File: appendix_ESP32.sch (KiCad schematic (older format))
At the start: 0 parts

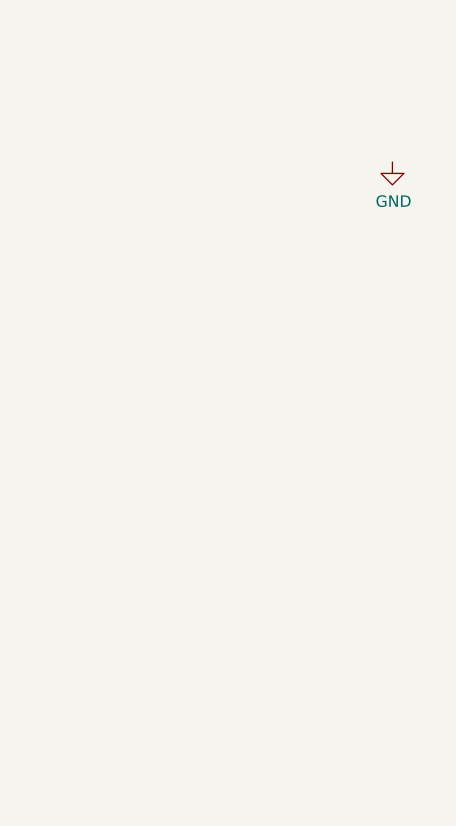
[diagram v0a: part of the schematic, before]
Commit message: added FTDI chip
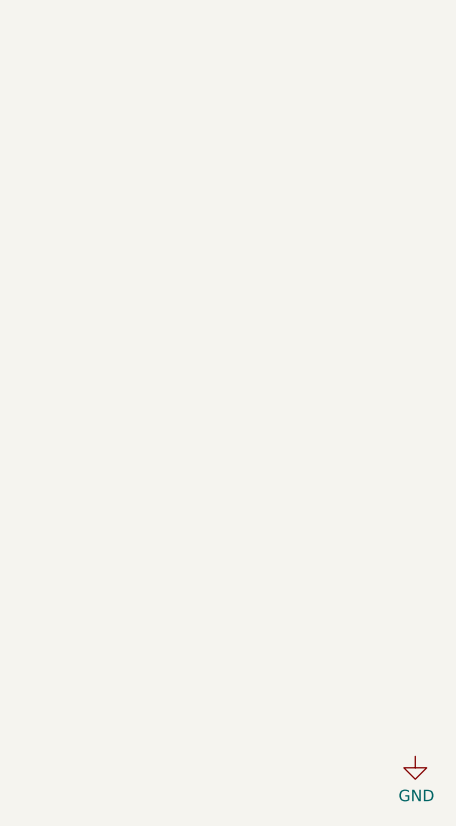
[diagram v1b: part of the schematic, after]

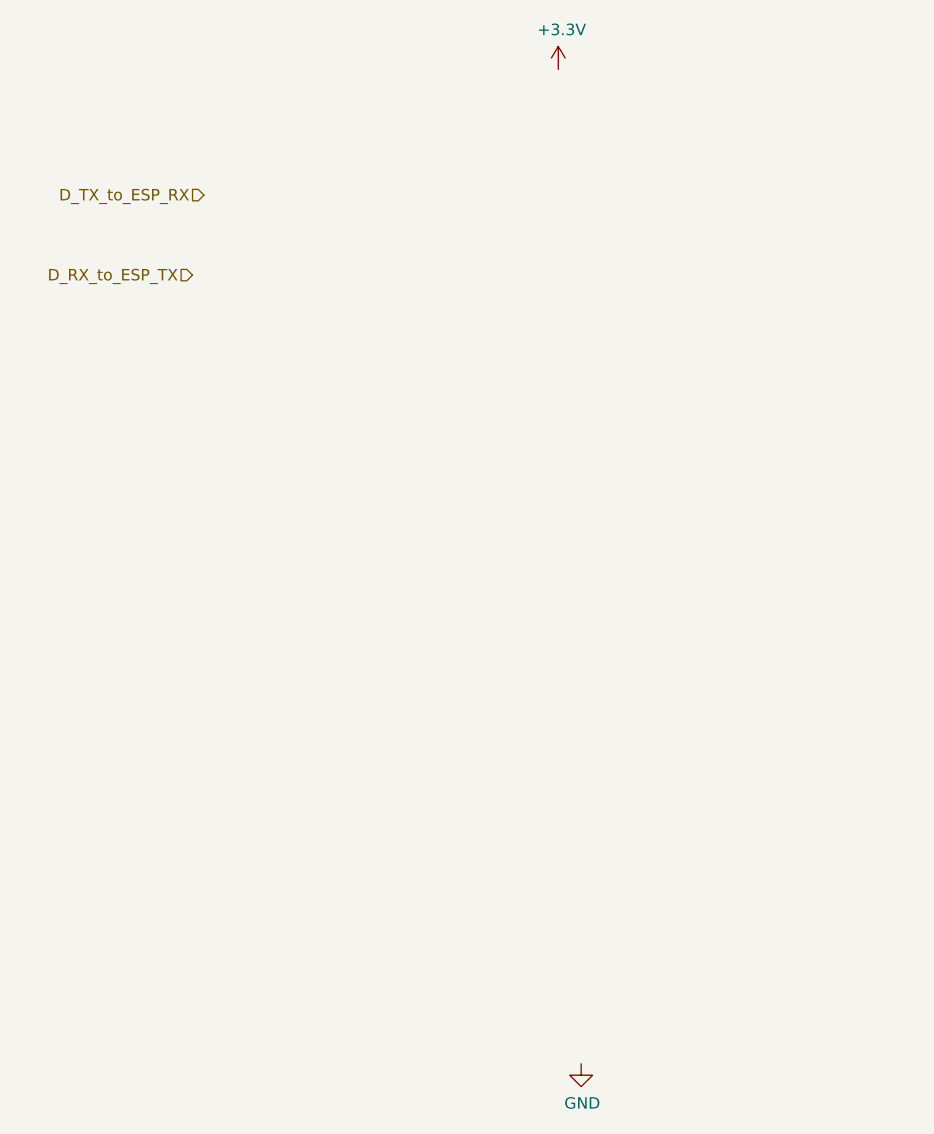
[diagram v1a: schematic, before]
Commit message: merged hierarchical schematics
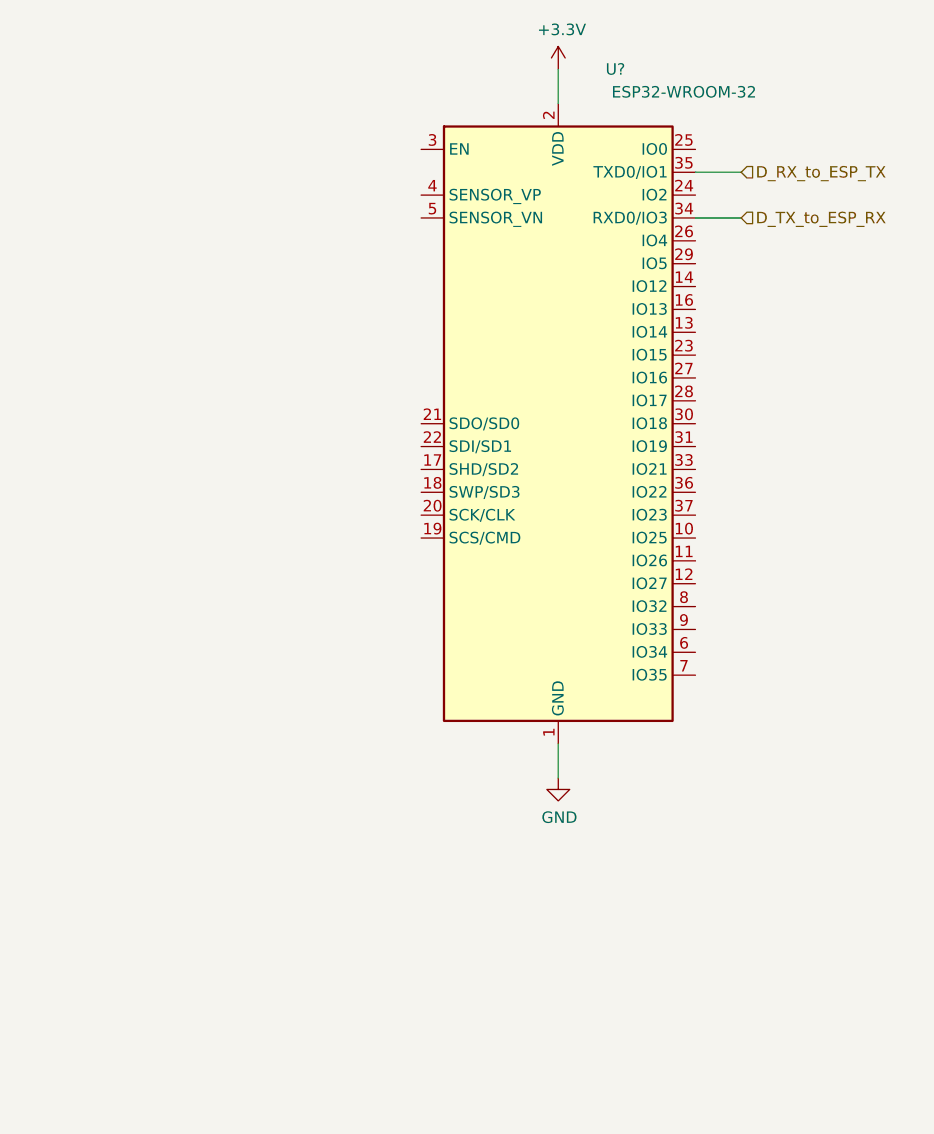
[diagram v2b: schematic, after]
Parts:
- added U?: ESP32-WROOM-32, RF_Module:ESP32-WROOM-32, symbol RF_Module:ESP32-WROOM-32
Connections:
- net +3V3: now also U?.2 (VDD)
- net D_RX_to_ESP_TX: now also U?.35 (TXD0/IO1)
- net D_TX_to_ESP_RX: now also U?.34 (RXD0/IO3)
- net GND: now also U?.1 (GND), U?.15 (GND), U?.38 (GND)
